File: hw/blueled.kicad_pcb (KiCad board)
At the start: 2 copper layers, 21.6 x 53.3 mm, 13 parts, among them J1 Barrel_Jack, J2 Screw_Terminal_01x03, U3 LM1117-3.3, X1 RESON-MURATA-CSTCE

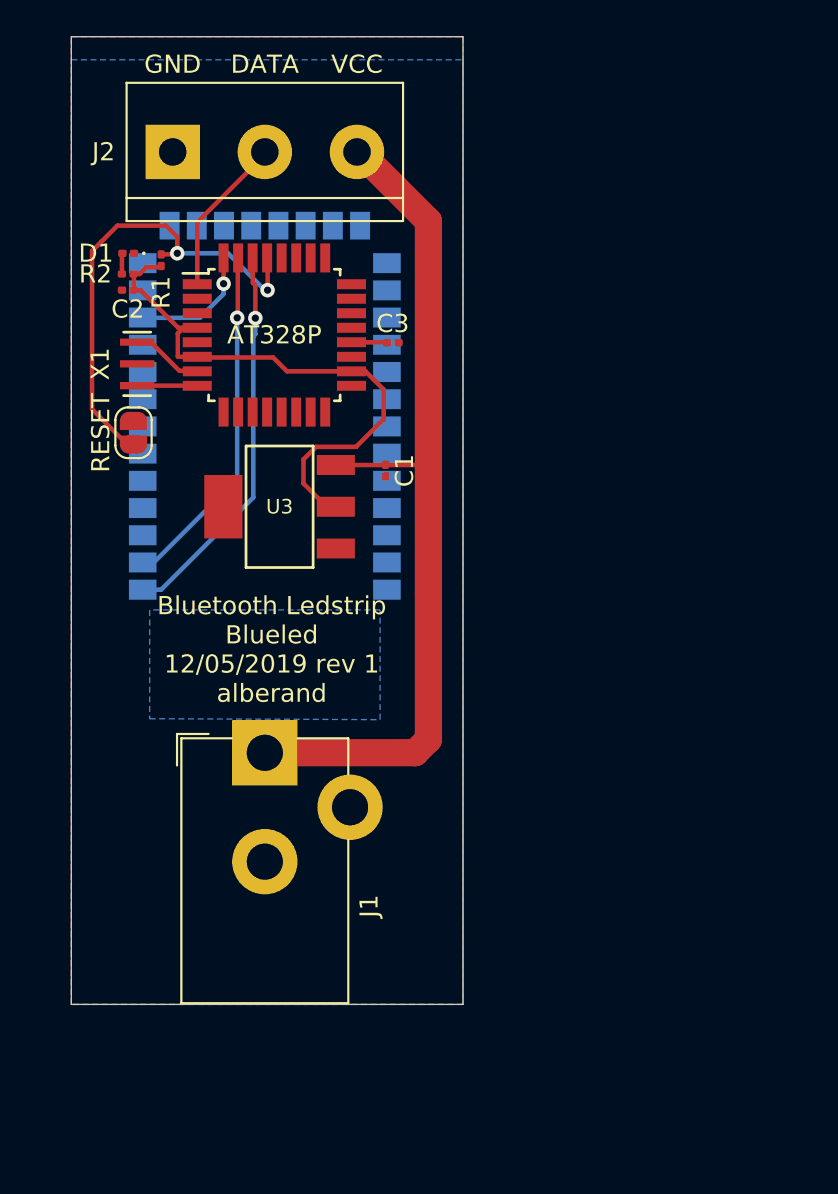
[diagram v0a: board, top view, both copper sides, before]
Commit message: hw: Get rid of "ambient" name -> now "blueled"
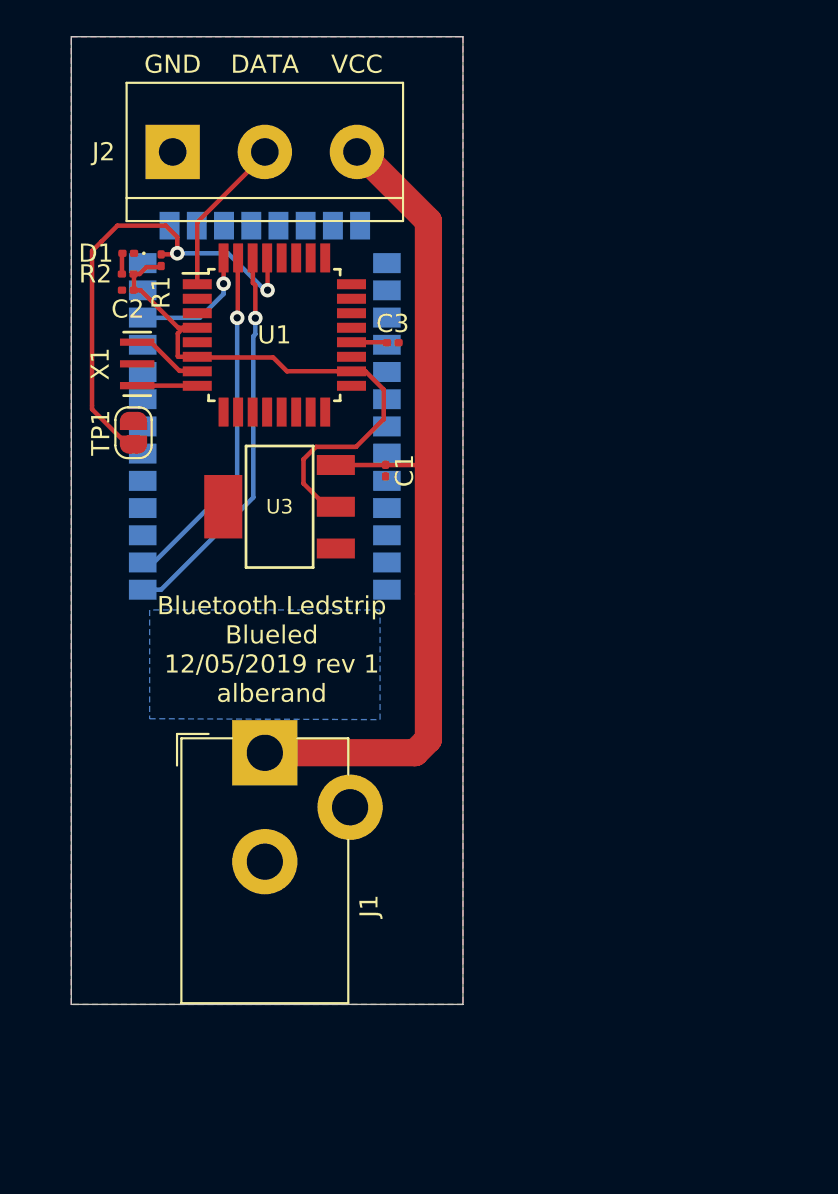
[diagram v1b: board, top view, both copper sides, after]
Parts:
- renumbered RESET to TP1, AT328P to U1, HC-05 to U2
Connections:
- J1 pad 3: GND -> (no net)
- U3 pad 4: GND -> (no net)
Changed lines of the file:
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@@
     (tags "QFP 0.8")
     (attr smd)
-    (fp_text reference AT328P (at 0 0) (layer F.SilkS)
+    (fp_text reference U1 (at 0 0) (layer F.SilkS)
       (effects (font (size 1 1) (thickness 0.15)))
     )
@@
     (tags "hc-05, bluetooth")
     (attr smd)
-    (fp_text reference HC-05 (at 0 0) (layer B.SilkS)
+    (fp_text reference U2 (at 0 0) (layer B.SilkS)
       (effects (font (size 1 1) (thickness 0.15)) (justify mirror))
     )
@@
       (effects (font (size 1 1) (thickness 0.15)))
     )
-    (pad 3 thru_hole circle (at 4.7 3) (size 3.6 3.6) (drill 2) (layers *.Cu *.Mask)
-      (net 54 GND))
+    (pad 3 thru_hole circle (at 4.7 3) (size 3.6 3.6) (drill 2) (layers *.Cu *.Mask))
     (pad 2 thru_hole circle (at 0 6) (size 3.6 3.6) (drill 2) (layers *.Cu *.Mask)
       (net 54 GND))
@@
     (pad 3 smd rect (at -3.1 2.3) (size 2.1 1.1) (layers F.Cu F.Paste F.Mask)
       (net 55 VIN))
-    (pad 4 smd rect (at 3.1 0) (size 2.1 3.5) (layers F.Cu F.Paste F.Mask)
-      (net 54 GND))
+    (pad 4 smd rect (at 3.1 0) (size 2.1 3.5) (layers F.Cu F.Paste F.Mask))
     (model smd_trans/sot223.wrl
       (at (xyz 0 0 0))
@@
     (tags "solder jumper open")
     (attr virtual)
-    (fp_text reference RESET (at 0 -1.8 90) (layer F.SilkS)
+    (fp_text reference TP1 (at 0 -1.8 90) (layer F.SilkS)
       (effects (font (size 1 1) (thickness 0.15)))
     )
@@
   (gr_line (start 142.24 97.79) (end 163.83 97.79) (layer Edge.Cuts) (width 0.05))
   (segment (start 145.6944 111.76) (end 145.6944 110.871) (width 0.25) (layer F.Cu) (net 1))
-  (segment (start 152.908 137.256) (end 154.458 137.256) (width 0.25) (layer F.Cu) (net 55))
   (segment (start 158.3436 116.2304) (end 154.1272 116.2304) (width 0.25) (layer F.Cu) (net 1))
   (segment (start 154.1272 116.2304) (end 153.3652 115.4684) (width 0.25) (layer F.Cu) (net 1))
@@
   (segment (start 145.669 110.871) (end 145.999 110.871) (width 0.25) (layer F.Cu) (net 1))
   (segment (start 146.38 110.49) (end 147.193 110.49) (width 0.25) (layer F.Cu) (net 1))
-  (segment (start 152.908 137.256) (end 161.194 137.256) (width 1.5) (layer F.Cu) (net 55))
-  (segment (start 161.194 137.256) (end 161.925 136.525) (width 1.5) (layer F.Cu) (net 55))
-  (segment (start 161.925 107.95) (end 158.115 104.14) (width 1.5) (layer F.Cu) (net 55))
   (segment (start 157.6848 114.632) (end 159.512 114.632) (width 0.25) (layer F.Cu) (net 2))
   (segment (start 159.512 114.632) (end 159.512 114.6048) (width 0.25) (layer F.Cu) (net 2))
@@
   (segment (start 149.1848 111.432) (end 149.1848 108.0156) (width 0.25) (layer F.Cu) (net 4))
   (segment (start 149.1848 108.0156) (end 152.9588 104.2416) (width 0.25) (layer F.Cu) (net 4))
-  (via (at 148.082 109.728) (size 0.8) (drill 0.4) (layers F.Cu B.Cu) (net 56))
-  (segment (start 147.943146 109.728) (end 148.082 109.728) (width 0.25) (layer F.Cu) (net 56))
-  (segment (start 148.082 109.728) (end 150.876 109.728) (width 0.25) (layer B.Cu) (net 56))
-  (segment (start 150.876 109.728) (end 152.908 111.76) (width 0.25) (layer B.Cu) (net 56))
-  (via (at 153.059003 111.76) (size 0.8) (drill 0.4) (layers F.Cu B.Cu) (net 56))
-  (segment (start 152.908 111.76) (end 153.059003 111.76) (width 0.25) (layer B.Cu) (net 56))
-  (segment (start 153.059003 111.76) (end 153.059003 110.49) (width 0.25) (layer F.Cu) (net 56))
   (segment (start 145.8722 114.624) (end 146.6222 114.624) (width 0.25) (layer F.Cu) (net 6))
   (segment (start 146.6222 114.624) (end 148.2032 116.205) (width 0.25) (layer F.Cu) (net 6))
@@
   (segment (start 150.6348 111.4044) (end 150.6348 111.970085) (width 0.25) (layer B.Cu) (net 27))
   (segment (start 149.320885 113.284) (end 146.4056 113.284) (width 0.25) (layer B.Cu) (net 27))
+  (segment (start 152.908 137.256) (end 154.458 137.256) (width 0.25) (layer F.Cu) (net 55))
+  (segment (start 152.908 137.256) (end 161.194 137.256) (width 1.5) (layer F.Cu) (net 55))
+  (segment (start 161.194 137.256) (end 161.925 136.525) (width 1.5) (layer F.Cu) (net 55))
+  (segment (start 161.925 107.95) (end 158.115 104.14) (width 1.5) (layer F.Cu) (net 55))
   (segment (start 161.8004 128.374) (end 161.925 128.4986) (width 0.25) (layer F.Cu) (net 55))
   (segment (start 161.925 136.525) (end 161.925 128.4986) (width 1.5) (layer F.Cu) (net 55))
@@
   (segment (start 161.925 128.4986) (end 161.925 120.9294) (width 1.5) (layer F.Cu) (net 55))
   (segment (start 161.925 120.9294) (end 161.925 107.95) (width 1.5) (layer F.Cu) (net 55))
+  (via (at 148.082 109.728) (size 0.8) (drill 0.4) (layers F.Cu B.Cu) (net 56))
+  (segment (start 147.943146 109.728) (end 148.082 109.728) (width 0.25) (layer F.Cu) (net 56))
+  (segment (start 148.082 109.728) (end 150.876 109.728) (width 0.25) (layer B.Cu) (net 56))
+  (segment (start 150.876 109.728) (end 152.908 111.76) (width 0.25) (layer B.Cu) (net 56))
+  (via (at 153.059003 111.76) (size 0.8) (drill 0.4) (layers F.Cu B.Cu) (net 56))
+  (segment (start 152.908 111.76) (end 153.059003 111.76) (width 0.25) (layer B.Cu) (net 56))
+  (segment (start 153.059003 111.76) (end 153.059003 110.49) (width 0.25) (layer F.Cu) (net 56))
   (segment (start 148.082 109.728) (end 148.082 108.839) (width 0.25) (layer F.Cu) (net 56))
   (segment (start 148.082 108.839) (end 147.447 108.204) (width 0.25) (layer F.Cu) (net 56))
@@
     (polygon
       (pts
-        (xy 163.83 151.13) (xy 142.24 151.13) (xy 142.24 99.06) (xy 163.83 99.06)
+        (xy 163.83 151.13) (xy 142.24 151.13) (xy 142.24 97.79) (xy 163.83 97.79)
       )
     )

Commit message: hw: Mainly refactoring + add switch to the schematics
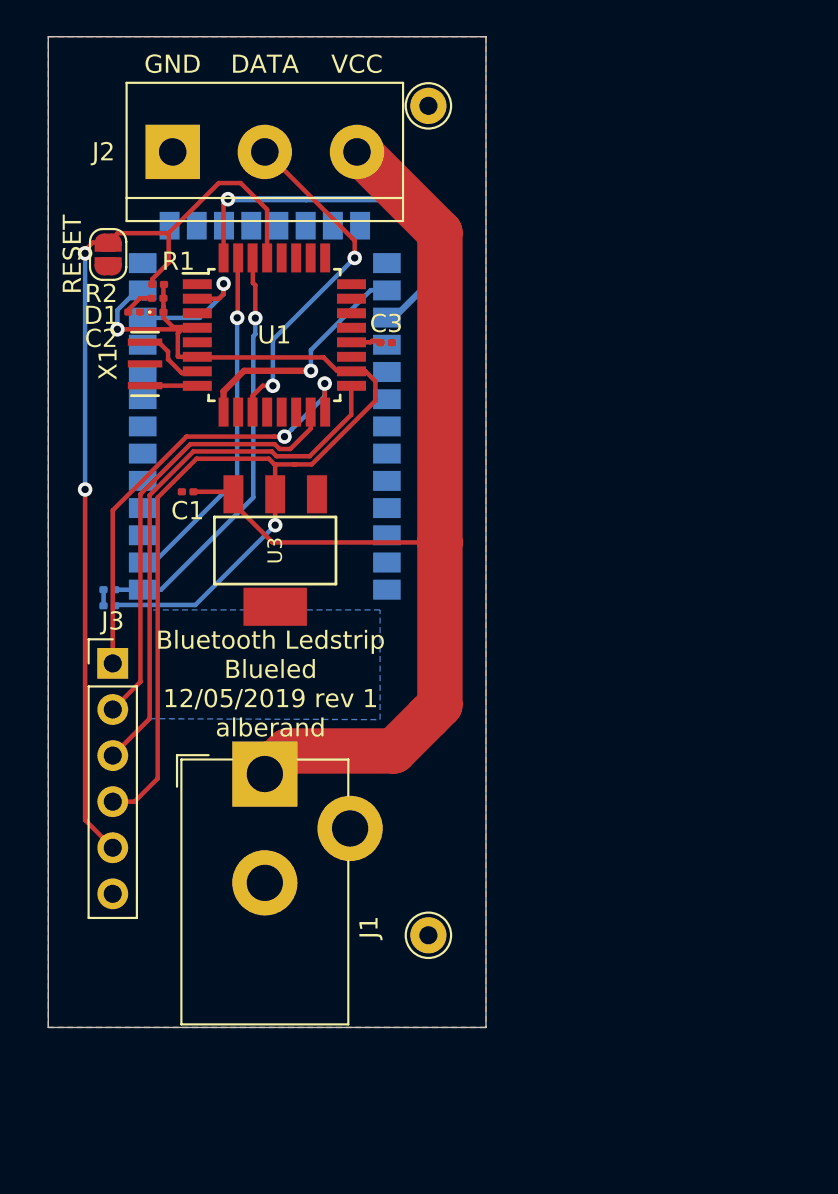
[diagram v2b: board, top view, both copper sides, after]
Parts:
- added D2: LED, LED_SMD:LED_0201_0603Metric, B.Cu at (144.3, 129.2)
- added Debug Handler: Pin_D1.0mm_L10.0mm, Connector_Pin:Pin_D1.0mm_L10.0mm, F.Cu at (161.9, 101.6)
- added J3: ICSP, Connector_PinHeader_2.54mm:PinHeader_1x06_P2.54mm_Vertical, F.Cu at (144.5, 132.3)
- added R3: 1k, Resistor_SMD:R_0201_0603Metric, B.Cu at (144.3, 128.3)
- added REF**: Pin_D1.0mm_L10.0mm, Connector_Pin:Pin_D1.0mm_L10.0mm, F.Cu at (161.9, 147.3)
- moved C1 11.0 mm to (148.7, 122.9), turned to 180 degrees
- moved RESET 9.93 mm to (144.3, 109.8), turned to 270 degrees
- moved D1 3.25 mm to (145.7, 113.0)
- moved U3 2.43 mm to (153.5, 126.1), turned to 270 degrees
- moved R2 2.12 mm to (147.0, 112.2)
- moved C2 2.04 mm to (147.0, 113.0)
- moved R1 1.34 mm to (147.0, 111.4), turned to 180 degrees
- moved J1 1.17 mm to (152.9, 138.4)
- moved X1 0.43 mm to (146.3, 115.8)
- moved C3 0.36 mm to (159.6, 114.7)
- renumbered U2 to HC-05, TP1 to RESET
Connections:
- net /RESET renamed RESET
- HC-05 pad 23: Net-(U2-Pad23) -> HC-DISCNCT
- HC-05 pad 24: Net-(U2-Pad24) -> HC-STATE
- HC-05 pad 34: Net-(U2-Pad34) -> HC-ATMODE
- U1 pad 1: DATA -> HC-ATMODE
- U1 pad 11: Net-(U1-Pad11) -> DATA
- U1 pad 15: Net-(U1-Pad15) -> MOSI
- U1 pad 16: Net-(U1-Pad16) -> MISO
- U1 pad 17: Net-(U1-Pad17) -> SCK
- U1 pad 2: Net-(U1-Pad2) -> HC-RESET
- U1 pad 32: HC-RESET -> HC-STATE
- U1 pad 9: Net-(U1-Pad9) -> HC-DISCNCT
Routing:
- net +3V3: track 31.2 -> 69.3 mm, vias 0 -> 2
- net SCK: track 0.00 -> 29.9 mm
- net RESET: track 26.0 -> 51.3 mm
- net MISO: track 0.00 -> 24.6 mm, vias 0 -> 2
- net MOSI: track 0.00 -> 24.1 mm
- net HC-STATE: track 0.00 -> 20.2 mm, vias 0 -> 1
- net HC-DISCNCT: track 0.00 -> 12.8 mm, vias 0 -> 1
- net DATA: track 8.75 -> 18.5 mm, vias 0 -> 2
- net VIN: track 50.3 -> 58.2 mm
- net RX: track 20.7 -> 21.8 mm
- net Net-(D2-Pad1): track 0.00 -> 0.83 mm
- net HC-RESET: track 6.76 -> 7.46 mm
- net Net-(U1-Pad8): track 2.82 -> 2.22 mm
- net Net-(D1-Pad2): track 1.08 -> 1.61 mm
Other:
- board size 21.6 x 53.3 mm -> 24.1 x 54.6 mm

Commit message: New version of hardware
* SPI chip is added but not routed
* Power switch MOSFET is added
* Power flags added
* SPI pins are moved to the right
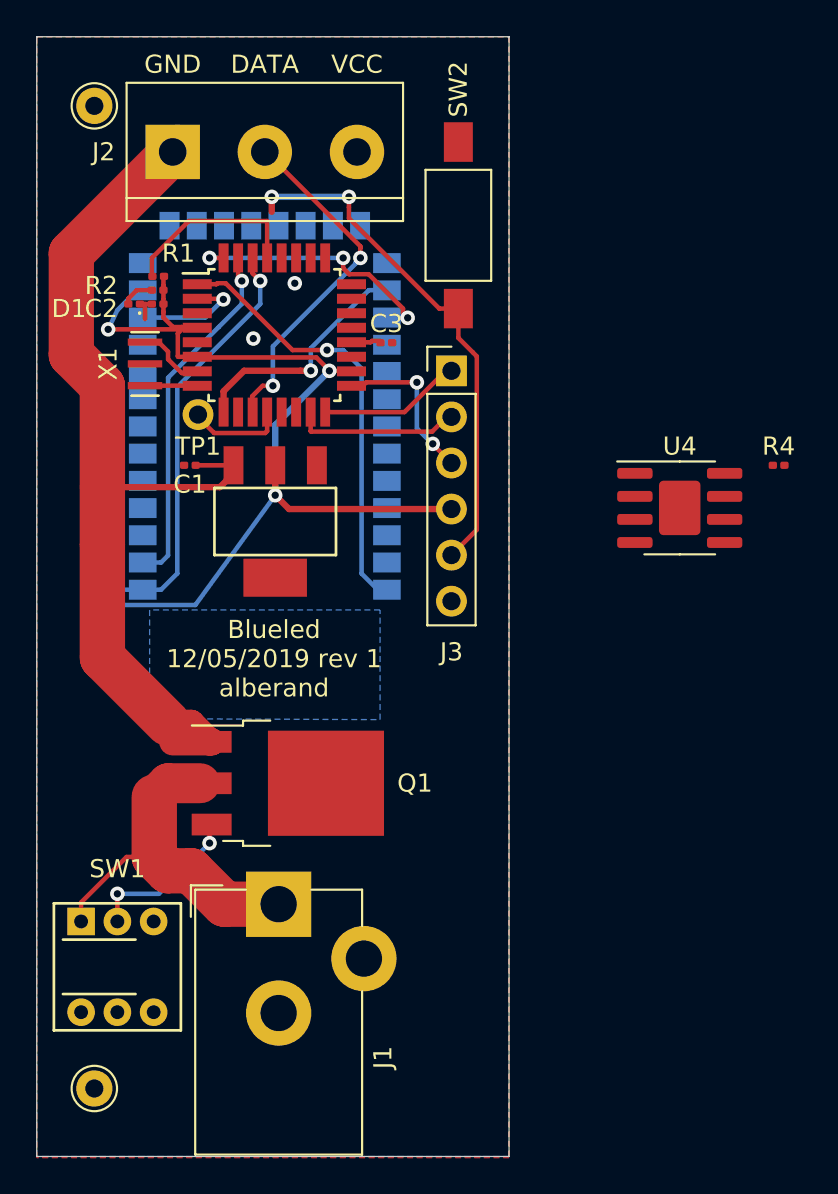
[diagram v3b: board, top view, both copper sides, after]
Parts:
- removed HC-05: HC-05, hc-05:HC-05
- removed RESET: TestPoint_2Pole, Jumper:SolderJumper-2_P1.3mm_Open_RoundedPad1.0x1.5mm
- added Q1: Q_PMOS_SDG, Package_TO_SOT_SMD:TO-252-3_TabPin4, F.Cu at (154.2, 138.9)
- added R4: 1k, Resistor_SMD:R_0201_0603Metric, F.Cu at (181.2, 121.4)
- added SW1: SW_Push_SPDT, USR-Footprints:XKB7070-Z, F.Cu at (144.8, 149.1)
- added SW2: PUSH, Button_Switch_SMD:SW_SPST_FSMSM, F.Cu at (163.6, 108.2)
- added TP1: Debug, TestPoint:TestPoint_THTPad_D1.0mm_Drill0.5mm, F.Cu at (149.2, 118.6)
- added U2: HC-05, USR-Footprints:HC-05, B.Cu at (152.9, 121.9)
- added U4: AT25DF512x-UxN-x, Package_SO:SOIC-8-1EP_3.9x4.9mm_P1.27mm_EP2.29x3mm, F.Cu at (175.8, 123.8)
- moved J3 24.7 mm to (163.2, 116.2)
- moved REF** 20.3 mm to (143.5, 155.8)
- moved Debug Handler 18.4 mm to (143.5, 101.6)
- moved J1 7.22 mm to (153.7, 145.6)
- moved U3 1.60 mm to (153.5, 124.5)
- moved C1 1.47 mm to (148.8, 121.4)
- moved C2 0.44 mm to (147.0, 112.5)
- moved D1 0.44 mm to (145.7, 112.5)
- moved R1 0.44 mm to (147.0, 111.0)
- moved R2 0.44 mm to (147.0, 111.8)
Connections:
- J1 pad 1: VIN -> /VINJACK
- J2 pad 1: GND -> VIN
- J2 pad 3: VIN -> GND
- U1 pad 14: Net-(U1-Pad14) -> FLASH_CSN
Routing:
- net HC-ATMODE: track 0.00 -> 23.8 mm, vias 0 -> 1
- net SCK: track 29.9 -> 8.40 mm, vias 0 -> 2
- net /VINJACK: track 0.00 -> 20.2 mm
- net MISO: track 24.6 -> 7.90 mm, vias 2 -> 0
- net +3V3: track 69.3 -> 52.9 mm, vias 2 -> 3
- net MOSI: track 24.1 -> 9.08 mm
- net RESET: track 51.3 -> 39.1 mm
- net Net-(Q1-Pad3): track 0.00 -> 8.52 mm, vias 0 -> 2
- net VIN: track 58.2 -> 50.8 mm
- net HC-STATE: track 20.2 -> 14.5 mm, vias 1 -> 3
- net Net-(TP1-Pad1): track 0.00 -> 5.45 mm
- net TX: track 18.1 -> 19.7 mm
- net GND: track 0.00 -> 1.42 mm, vias 0 -> 1
- net HC-RESET: track 7.46 -> 6.31 mm
- net RX: track 21.8 -> 22.8 mm
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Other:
- board size 24.1 x 54.6 mm -> 26 x 61.7 mm
- board text added: "Blueled 12/05/2019 rev 1 alberand"
- board text removed: "Bluetooth Ledstrip Blueled 12/05/2019 rev 1 alberand"

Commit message: Make pads for SMD components bigger and general rerouting
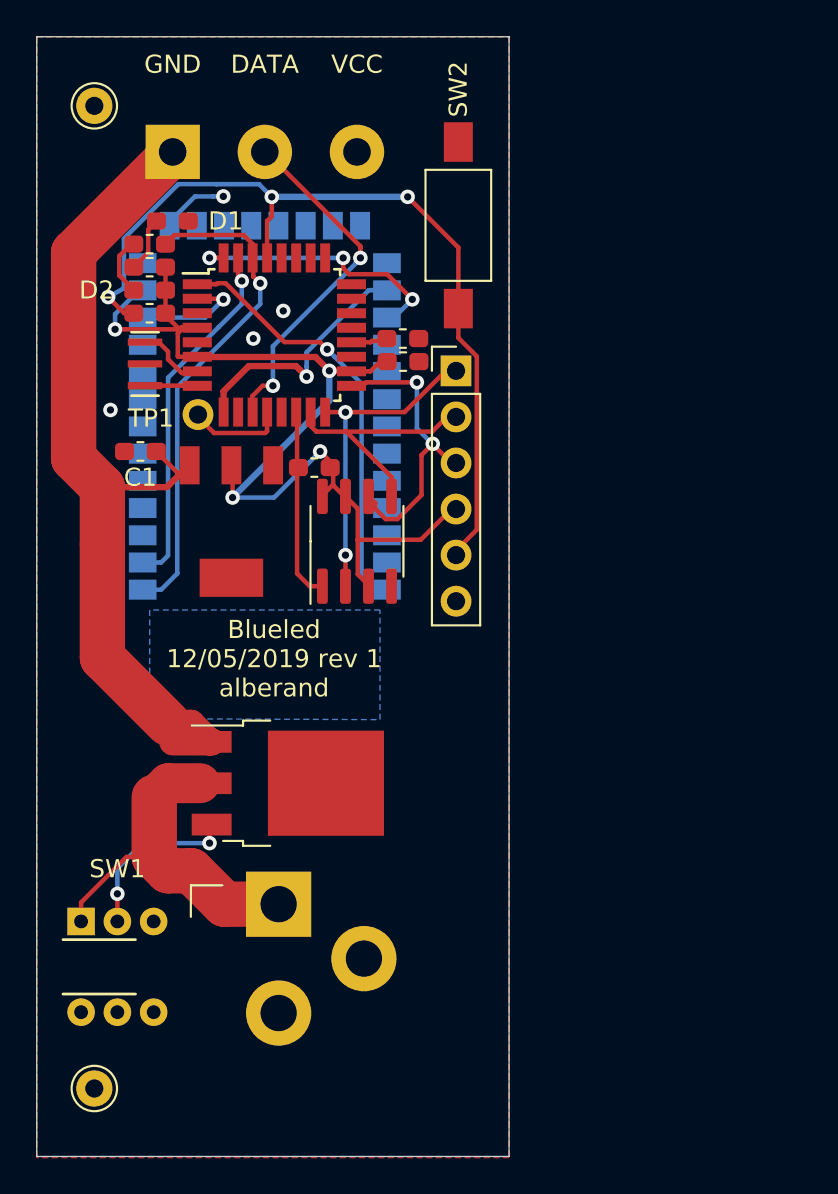
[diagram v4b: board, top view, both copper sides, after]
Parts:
- C1, C2, C3: footprint Capacitor_SMD:C_0201_0603Metric -> Capacitor_SMD:C_0603_1608Metric_Pad1.05x0.95mm_HandSolder
- D1: footprint LED_SMD:LED_0201_0603Metric -> LED_SMD:LED_0603_1608Metric_Pad1.05x0.95mm_HandSolder
- D2: footprint LED_SMD:LED_0201_0603Metric -> LED_SMD:LED_0603_1608Metric_Pad1.05x0.95mm_HandSolder; moved to F.Cu
- R1, R2, R4: footprint Resistor_SMD:R_0201_0603Metric -> Resistor_SMD:R_0603_1608Metric_Pad1.05x0.95mm_HandSolder
- R3: footprint Resistor_SMD:R_0201_0603Metric -> Resistor_SMD:R_0603_1608Metric_Pad1.05x0.95mm_HandSolder; moved to F.Cu
- moved R4 25.6 mm to (155.6, 121.5), turned to 180 degrees
- moved R3 19.2 mm to (146.6, 109.2)
- moved U4 17.9 mm to (158.0, 125.6), turned to 90 degrees
- moved D2 17.5 mm to (146.6, 111.8)
- moved C2 13.9 mm to (160.5, 115.7), turned to 0 degrees
- moved D1 5.03 mm to (147.8, 108.0)
- moved C1 2.83 mm to (146.1, 120.7)
- moved U3 2.41 mm to (151.1, 124.5)
- moved R1 2.09 mm to (146.6, 113.0)
- moved R2 1.34 mm to (146.6, 110.5)
- moved C3 0.94 mm to (160.5, 114.4)
- moved J3 0.25 mm to (163.4, 116.2)
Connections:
- U4 pad 1: (no net) -> FLASH_CSN
- U4 pad 2: (no net) -> MISO
- U4 pad 3: (no net) -> +3V3
- U4 pad 4: (no net) -> GND
- U4 pad 5: (no net) -> MOSI
- U4 pad 6: (no net) -> SCK
- U4 pad 7: (no net) -> +3V3
- U4 pad 8: (no net) -> +3V3
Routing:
- net FLASH_CSN: track 0.00 -> 10.4 mm
- net MISO: track 7.90 -> 17.5 mm, vias 0 -> 2
- net RESET: track 39.1 -> 48.0 mm, vias 2 -> 3
- net SCK: track 8.40 -> 15.6 mm
- net MOSI: track 9.08 -> 13.5 mm
- net RX: track 22.8 -> 26.8 mm
- net VIN: track 50.8 -> 48.0 mm
- net +3V3: track 52.9 -> 55.5 mm, vias 3 -> 4
- net GND: track 1.42 -> 3.76 mm, vias 1 -> 4
- net Net-(D2-Pad1): track 0.83 -> 2.97 mm
- net Net-(D1-Pad2): track 1.79 -> 3.49 mm
- net Net-(Q1-Pad3): track 8.52 -> 9.34 mm
- net HC-STATE: track 14.5 -> 15.3 mm
- net HC-DISCNCT: track 12.8 -> 13.3 mm
- net (no net): vias 1 -> 0
